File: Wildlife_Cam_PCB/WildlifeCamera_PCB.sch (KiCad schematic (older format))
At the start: 47 parts, among them J1 PIR, J2 TRIG, J3 RTC_DS3231, J4 PROG, J5 PROG_EN, J6 LOGO1, J7 LOGO2, J8 PCB, J9 PV, Q1 2N3904, Q2 2N3904, Q3 BD135, SW1 ON/OFF, SW2 TRIGGER, U1 MCP1826S-3302, U2 BQ24210, U3 ESP32_CAM

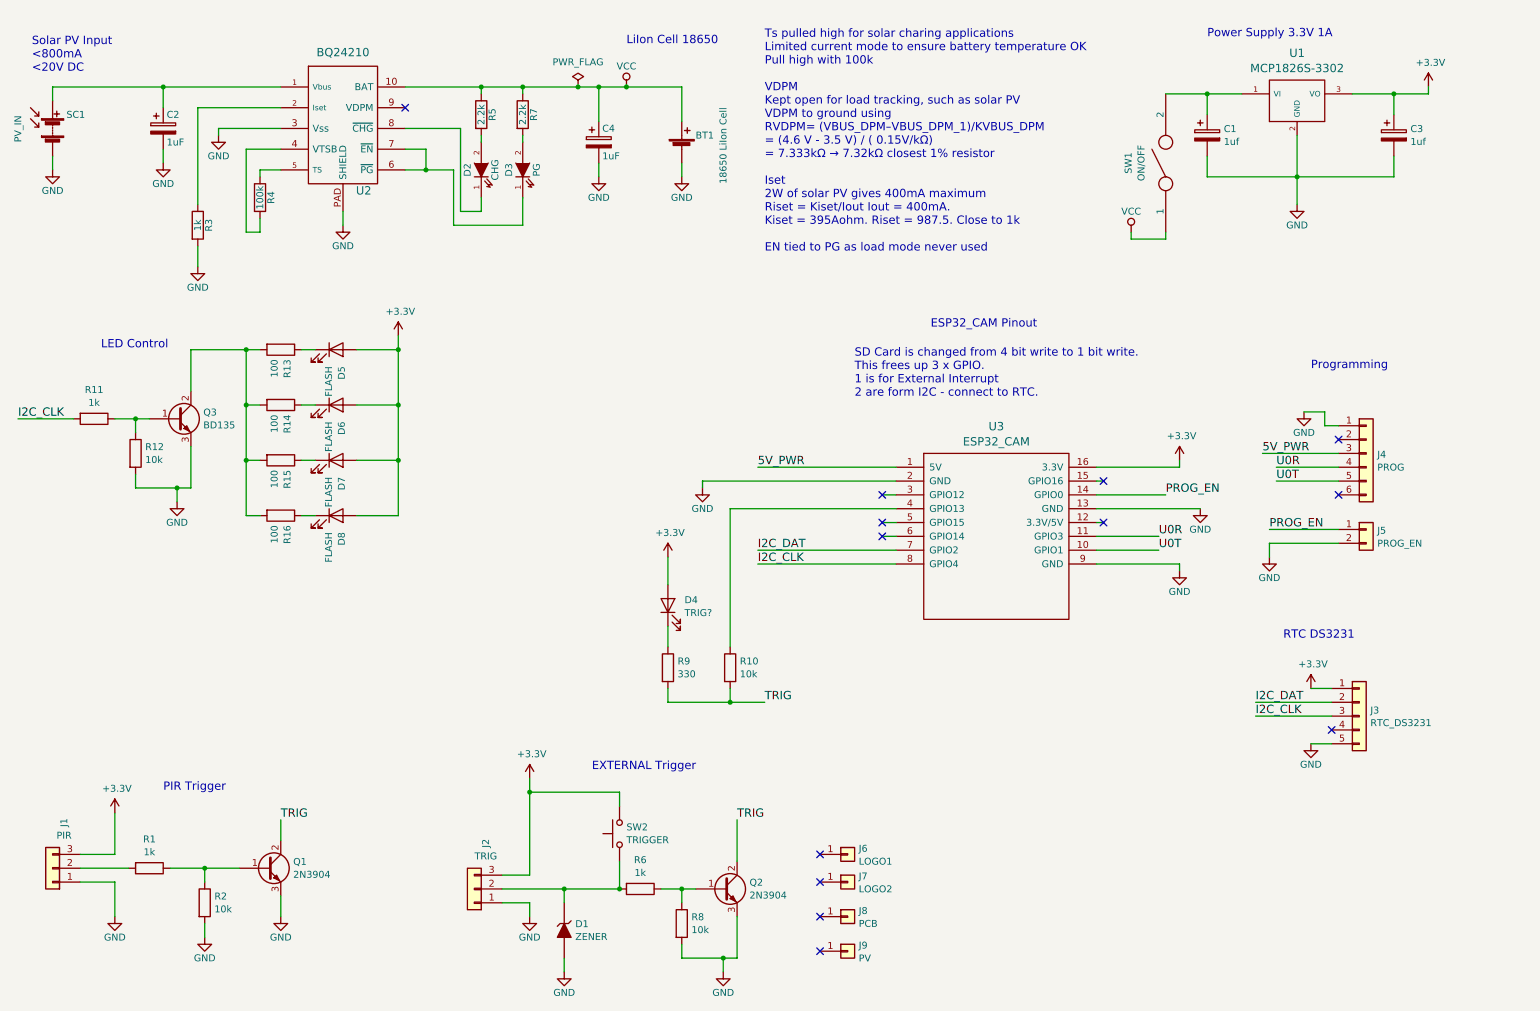
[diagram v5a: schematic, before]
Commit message: Update of code - sorting libraries
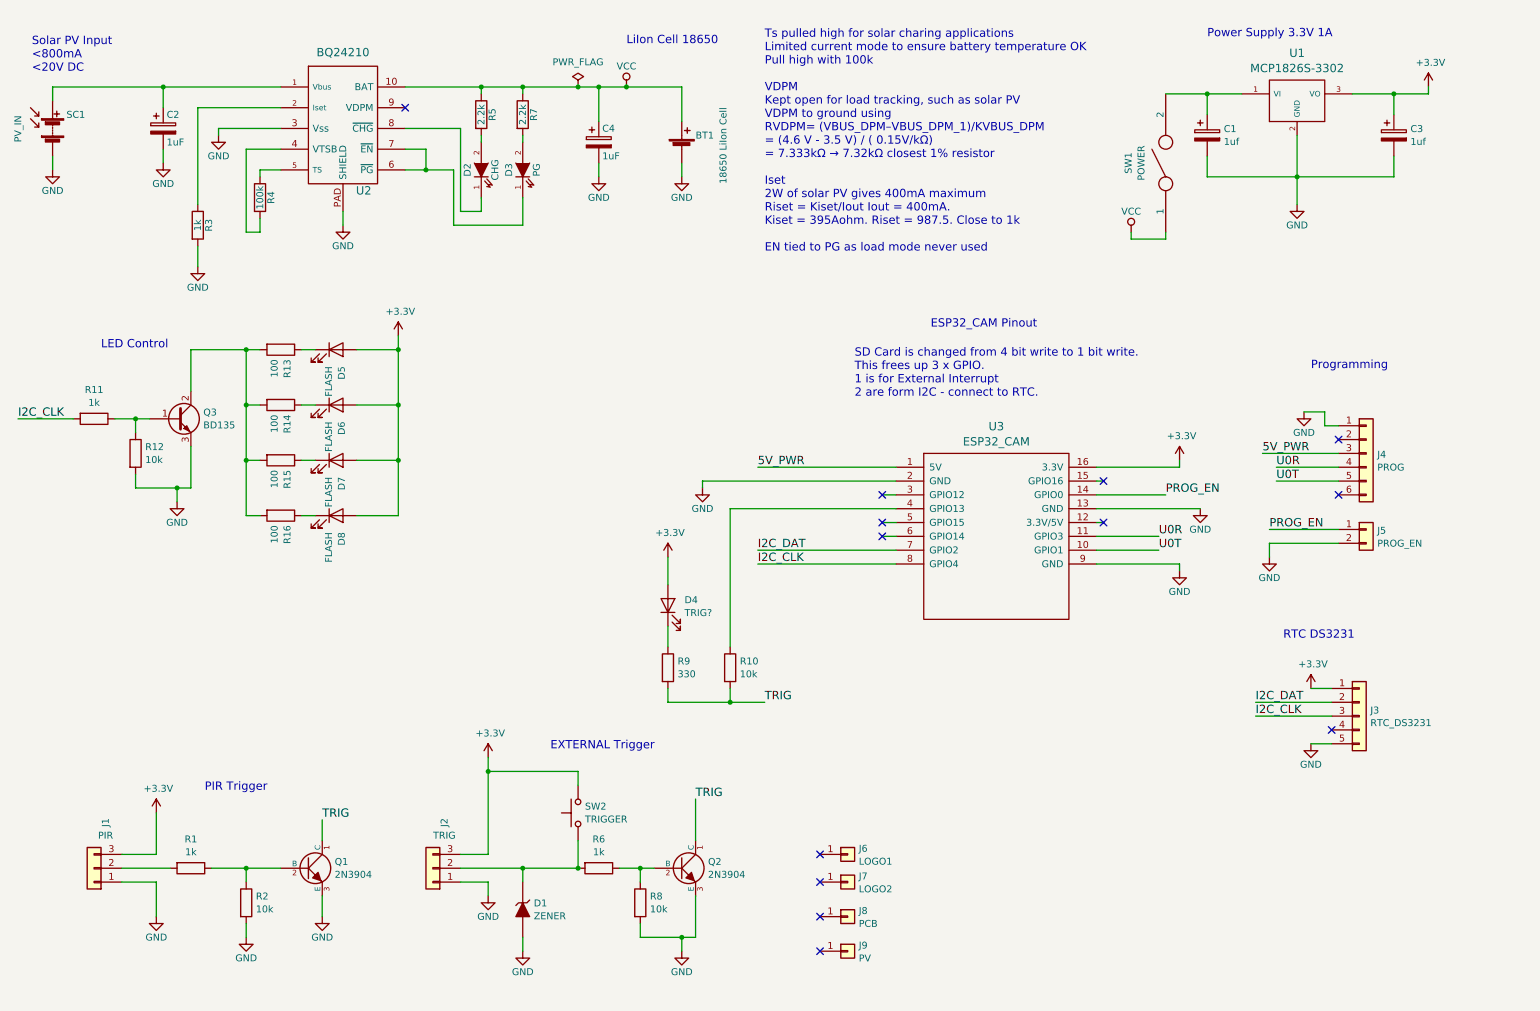
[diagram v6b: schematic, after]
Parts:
- removed Q1, Q2: 2N3904, REInnovationFootprint:TO92-EBC_large_pad, symbol WildlifeCamera_PCB-rescue:Q_NPN_BCE-Device
- added Q1, Q2: 2N3904, REInnovationFootprint:NPN_BC337, symbol matts_components:NPN
- J1: footprint REInnovationFootprint:SIL-3_lg_pad -> REInnovationFootprint:SIL-3_PIR_SENSOR
- SW1: value ON/OFF -> POWER
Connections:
- net GND: now also Q1.3 (E), Q2.3 (E)
- net TRIG: now also Q1.1 (C), Q2.1 (C)
- net at R1.1, R2.1: now also Q1.2 (B)
- net at R6.1, R8.1: now also Q2.2 (B)
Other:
- moved on the sheet: D1, J1, J2, R1, R2, R6, R8, SW2
